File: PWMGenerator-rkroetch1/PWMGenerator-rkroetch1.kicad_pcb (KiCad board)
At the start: 2 copper layers, 0 parts

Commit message: Update Jack footprint, finish part 2
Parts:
- added C1: 220uF, Capacitor_THT:CP_Radial_D8.0mm_P3.50mm, F.Cu at (103.5, 58.9)
- added C2: 10uF, Capacitor_THT:CP_Radial_D10.0mm_P5.00mm, F.Cu at (114.7, 58.9)
- added C3: 0.1uF, Capacitor_SMD:C_0805_2012Metric, F.Cu at (111.8, 80.3)
- added D1: 1N4005G, Diode_THT:D_DO-41_SOD81_P10.16mm_Horizontal, F.Cu at (75.7, 73.2)
- added D2: 1N4005G, Diode_THT:D_DO-41_SOD81_P10.16mm_Horizontal, F.Cu at (75.7, 100.1)
- added D3: 1N4005G, Diode_THT:D_DO-41_SOD81_P10.16mm_Horizontal, F.Cu at (87.9, 83.3)
- added D4: 1N4005G, Diode_THT:D_DO-41_SOD81_P10.16mm_Horizontal, F.Cu at (87.9, 89.9)
- added D5: 1N4005G, Diode_THT:D_DO-41_SOD81_P10.16mm_Horizontal, F.Cu at (96.0, 73.2)
- added D6: LED_GREEN, LED_THT:LED_D5.0mm, F.Cu at (88.4, 47.2)
- added F1: NANOSMDC016F-2, Library:RESC3115X65N, F.Cu at (75.7, 65.5)
- added J1: Conn_01x03_Pin, Connector_PinHeader_2.54mm:PinHeader_1x03_P2.54mm_Vertical, F.Cu at (141.7, 61.5)
- added Q1: 2N3904, Package_TO_SOT_THT:TO-92_Inline, F.Cu at (102.1, 95.5)
- added Q2: 2N3904, Package_TO_SOT_THT:TO-92_Inline, F.Cu at (102.1, 87.4)
- added Q3: 2N3906, Package_TO_SOT_THT:TO-92_Inline, F.Cu at (114.3, 87.4)
- added Q4: 2N3906, Package_TO_SOT_THT:TO-92_Inline, F.Cu at (114.3, 95.5)
- added R1: 2.2k, Resistor_SMD:R_0805_2012Metric, F.Cu at (95.9, 95.5)
- added R10: 8.2k, Resistor_SMD:R_0805_2012Metric, F.Cu at (116.3, 80.3)
- added R11: 180, Resistor_SMD:R_0805_2012Metric, F.Cu at (116.4, 74.7)
- added R2: 1M, Resistor_SMD:R_0805_2012Metric, F.Cu at (95.9, 89.4)
- added R3: 330, Resistor_SMD:R_0805_2012Metric, F.Cu at (97.0, 47.2)
- added R4: 10k, Resistor_SMD:R_0805_2012Metric, F.Cu at (102.6, 74.7)
- added R5: 220k, Resistor_SMD:R_0805_2012Metric, F.Cu at (107.2, 74.7)
- added R6: 390k, Resistor_SMD:R_0805_2012Metric, F.Cu at (107.2, 80.3)
- added R7: 22k, Resistor_SMD:R_0805_2012Metric, F.Cu at (102.6, 80.3)
- added R8: 2.2k, Resistor_SMD:R_0805_2012Metric, F.Cu at (111.9, 74.7)
- added R9: 5k, Potentiometer_THT:Potentiometer_Piher_PT-15-V15_Vertical_Hole, F.Cu at (127.0, 53.8)
- added SW1: AS11CP, Library:SW_AS11CP, F.Cu at (89.9, 59.4)
- added U1: LM7805_TO220, Package_TO_SOT_THT:TO-220-3_Vertical, F.Cu at (107.2, 47.2)
- added U2: LM339AJ, Package_SO:SOIC-14_3.9x8.7mm_P1.27mm, F.Cu at (124.5, 69.8)
- added V1: Barrel_Jack, Connector_BarrelJack:BarrelJack_SwitchcraftConxall_RAPC10U_Horizontal, F.Cu at (80.8, 47.8)
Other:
- board outline added: 81.8 x 65.4 mm

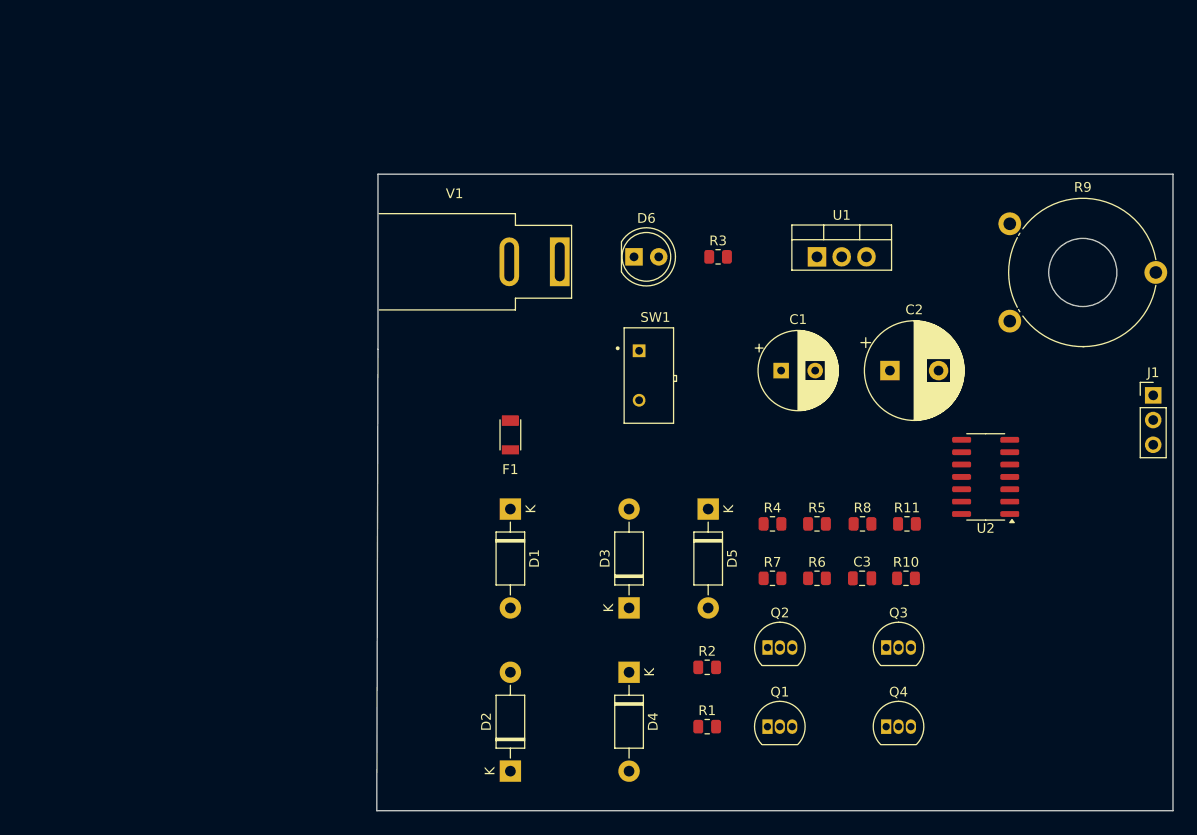
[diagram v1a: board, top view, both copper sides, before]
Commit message: Fill zones
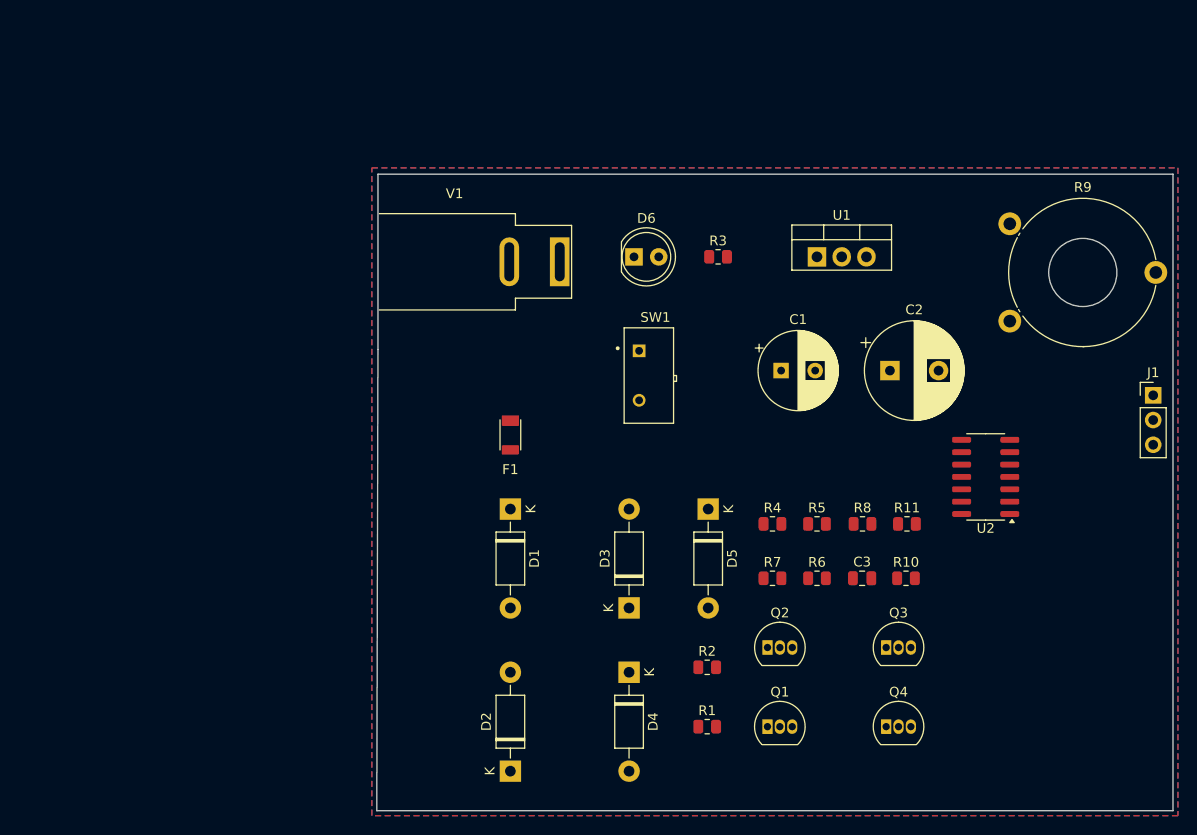
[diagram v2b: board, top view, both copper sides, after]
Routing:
- added copper zone on B.Cu, net GND
- added copper zone on F.Cu, net VCC
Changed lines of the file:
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@@
 		(layer "Edge.Cuts")
+	)
+	(zone
+		(net 1)
+		(net_name "VCC")
+		(layer "F.Cu")
+		(hatch edge 0.5)
+		(priority 1)
+		(connect_pads
+			(clearance 0.5)
+		)
+		(min_thickness 0.25)
+		(filled_areas_thickness no)
+		(fill yes
+			(mode hatch)
+			(thermal_gap 0.5)
+			(thermal_bridge_width 0.5)
+			(hatch_thickness 1)
+			(hatch_gap 1.5)
+			(hatch_orientation 0)
+			(hatch_border_algorithm hatch_thickness)
+			(hatch_min_hole_area 0.3)
+		)
+		(polygon
+			(pts
+				(xy 61.468 38.1) (xy 144.272 38.1) (xy 144.272 104.648) (xy 61.468 104.648)
+			)
+		)
+	)
+	(zone
+		(net 2)
+		(net_name "GND")
+		(layer "B.Cu")
+		(hatch edge 0.5)
+		(connect_pads
+			(clearance 0.5)
+		)
+		(min_thickness 0.25)
+		(filled_areas_thickness no)
+		(fill yes
+			(mode hatch)
+			(thermal_gap 0.5)
+			(thermal_bridge_width 0.5)
+			(hatch_thickness 1)
+			(hatch_gap 1.5)
+			(hatch_orientation 0)
+			(hatch_border_algorithm hatch_thickness)
+			(hatch_min_hole_area 0.3)
+		)
+		(polygon
+			(pts
+				(xy 61.468 38.1) (xy 144.272 38.1) (xy 144.272 104.648) (xy 61.468 104.648)
+			)
+		)
 	)
 	(embedded_fonts no)

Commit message: No errors/warnings
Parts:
- moved Q4 39.1 mm to (131.3, 60.3)
- moved R11 23.6 mm to (136.9, 62.8), turned to -90 degrees
- moved R7 19.8 mm to (119.9, 70.6), turned to -90 degrees
- moved R10 16.8 mm to (131.6, 73.2)
- moved R8 15.4 mm to (123.4, 64.5), turned to -90 degrees
- moved Q2 13.5 mm to (106.7, 74.7), turned to 90 degrees
- moved R6 12.7 mm to (118.4, 86.4), turned to -90 degrees
- moved Q1 12.2 mm to (102.6, 83.3), turned to 90 degrees
- moved Q3 9.86 mm to (116.3, 77.7), turned to 180 degrees
- moved U2 9.46 mm to (123.4, 79.2)
- moved R5 8.63 mm to (114.8, 70.6), turned to -90 degrees
- moved C2 6.52 mm to (109.2, 55.4)
- moved U1 5.93 mm to (104.1, 42.2)
- moved R4 5.50 mm to (99.6, 70.1), turned to -90 degrees
- moved R3 5.01 mm to (95.0, 51.8), turned to 90 degrees
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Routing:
- net Net-(J1-Pin_1): track 0.00 -> 121.3 mm
- net GNDPWR: track 0.00 -> 72.7 mm
- net VCC: track 0.00 -> 54.7 mm
- net GND: track 0.00 -> 44.7 mm, vias 0 -> 13
- net Net-(Q2-C): track 0.00 -> 40.1 mm
- net Net-(U2A-+): track 0.00 -> 30.8 mm
- net Net-(D3-K): track 0.00 -> 26.5 mm
- net Net-(D1-K): track 0.00 -> 19.7 mm
- net Net-(Q1-C): track 0.00 -> 19.1 mm
- net Net-(Q3-B): track 0.00 -> 15.4 mm
- net Net-(SW1-Pad1): track 0.00 -> 15.2 mm
- net Net-(F1-Pad1): track 0.00 -> 15.0 mm
- net Net-(Q4-B): track 0.00 -> 12.9 mm
- net Net-(R10-Pad1): track 0.00 -> 11.2 mm
- net Net-(J1-Pin_2): track 0.00 -> 10.6 mm
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
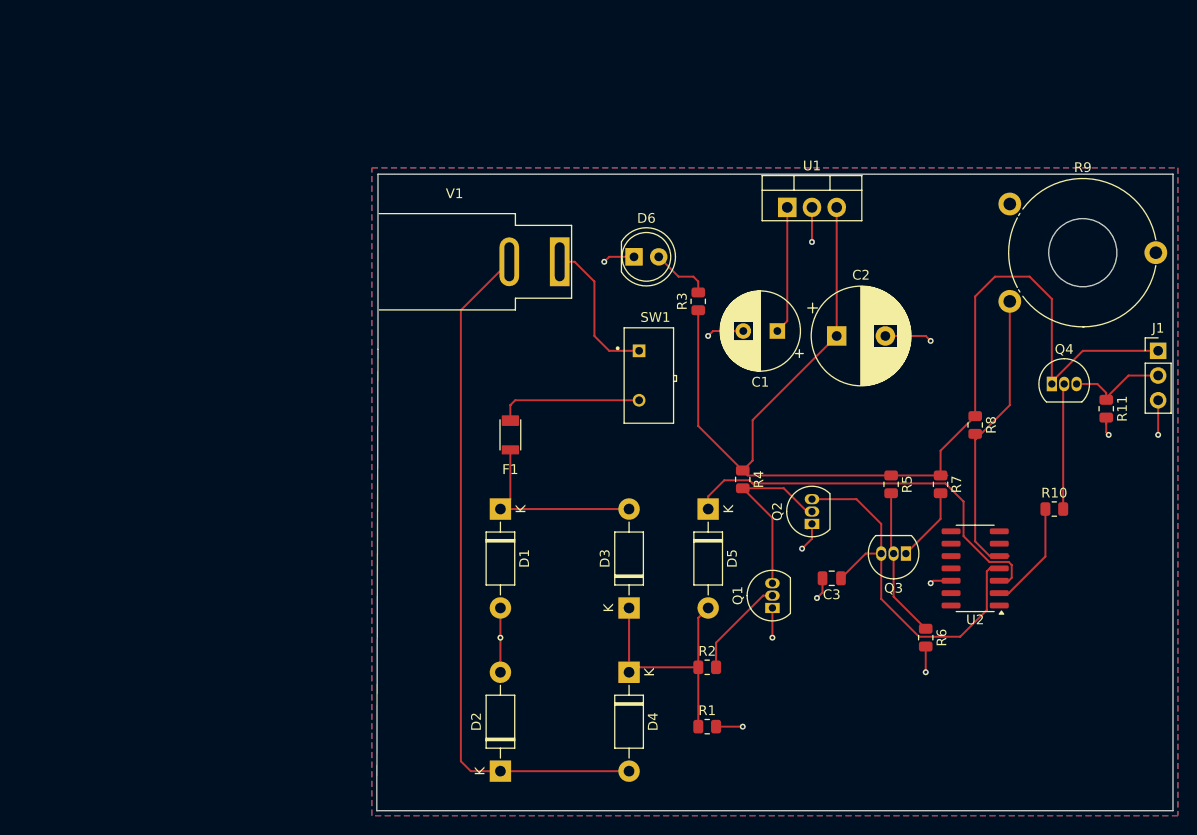
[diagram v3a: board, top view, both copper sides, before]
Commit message: Aligned text a little better
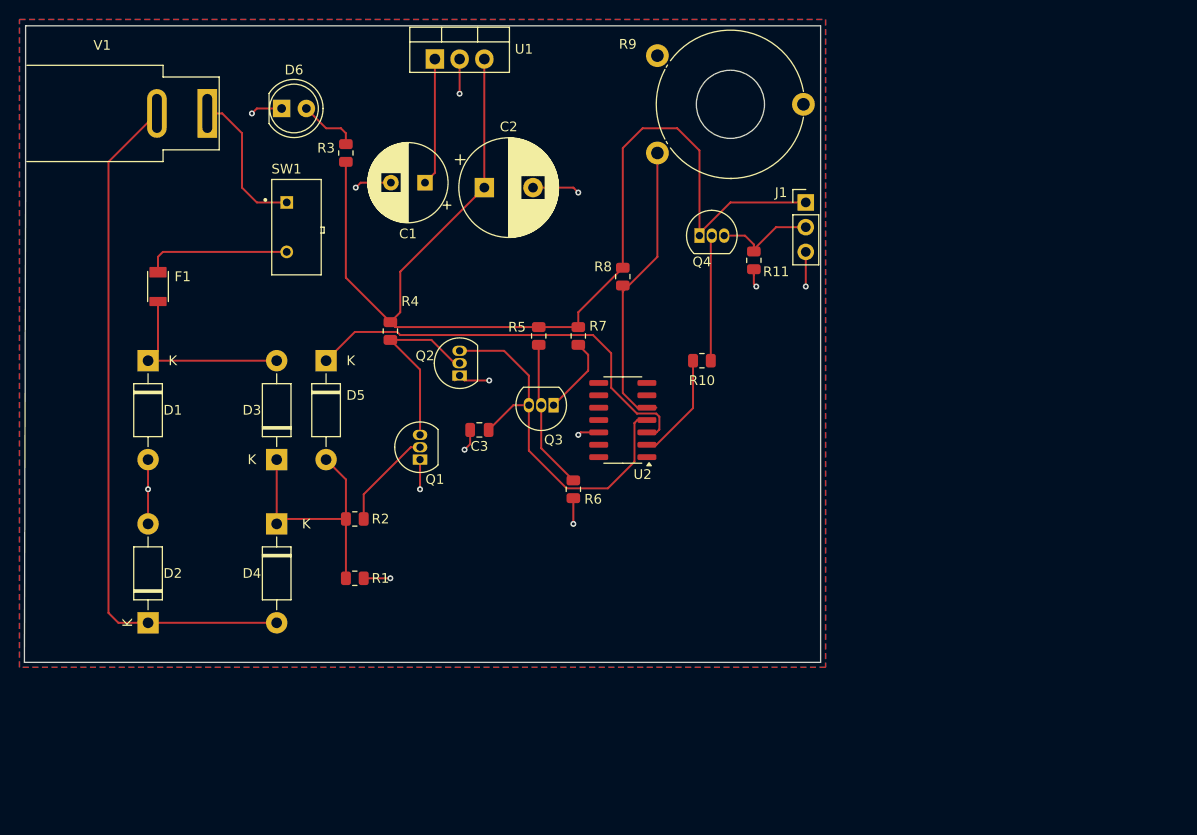
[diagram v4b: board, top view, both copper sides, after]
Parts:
- moved D5 42.1 mm to (56.8, 57.9)
- moved R7 40.2 mm to (82.7, 55.4)
- moved J1 39.3 mm to (106.0, 41.7)
- moved Q2 39.3 mm to (70.5, 59.4)
- moved Q4 39.3 mm to (95.1, 45.1)
- moved R10 39.3 mm to (95.4, 57.9)
- moved R11 39.3 mm to (100.7, 47.6)
- moved R8 39.3 mm to (87.2, 49.3)
- moved U2 39.3 mm to (87.2, 64.0)
- moved V1 39.3 mm to (44.6, 32.5)
- moved C3 39.3 mm to (72.5, 65.0)
- moved D1 39.3 mm to (38.5, 57.9)
- moved D2 39.3 mm to (38.5, 84.8)
- moved D3 39.3 mm to (51.7, 68.1)
- moved D4 39.3 mm to (51.7, 74.7)
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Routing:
- net VCC: track 54.7 -> 57.0 mm
- net Net-(J1-Pin_1): track 121.3 -> 120.1 mm
